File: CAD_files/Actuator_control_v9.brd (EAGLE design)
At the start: 33.5 x 16 mm, 35 parts, among them Y1 16MHz

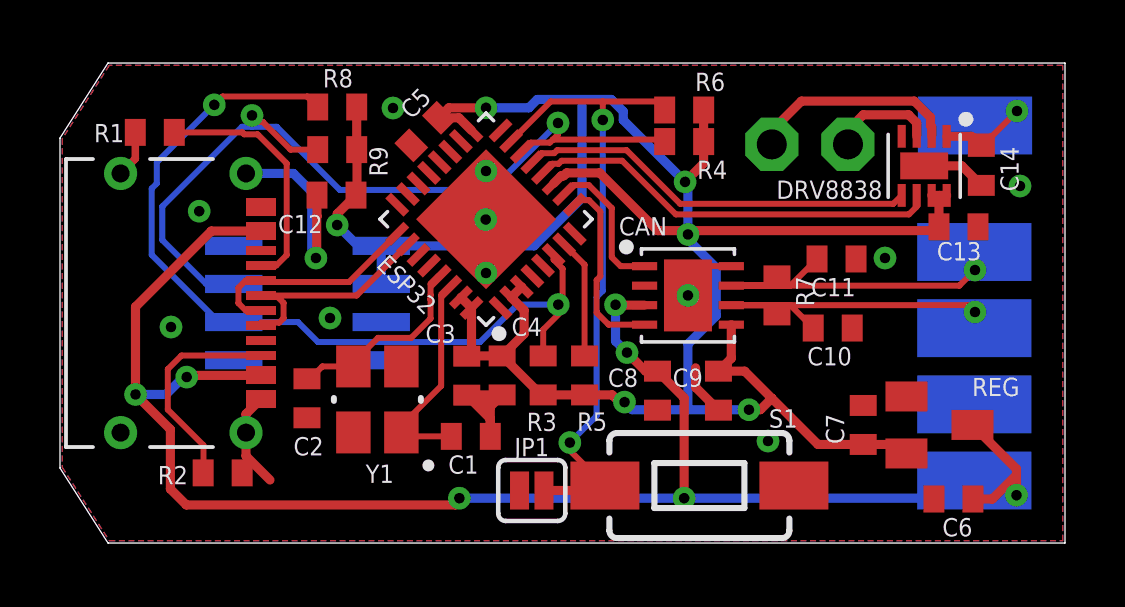
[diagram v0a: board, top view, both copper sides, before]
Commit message: Resolved issue #9
Removed CAN lines capacitors and added info regarding terminating resistors
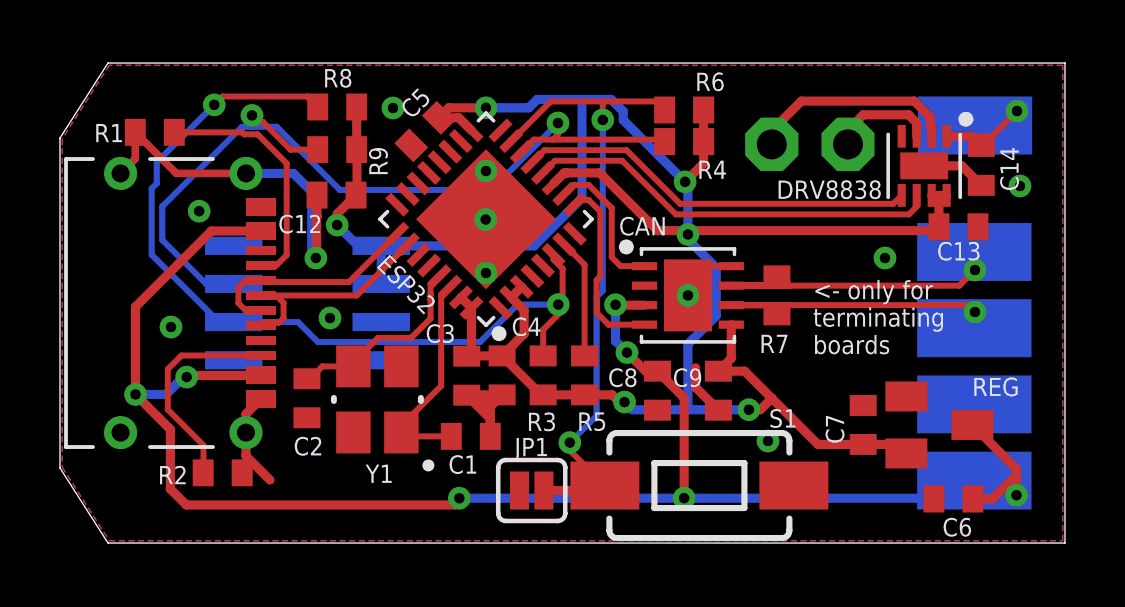
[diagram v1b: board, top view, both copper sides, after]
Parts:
- removed C10, C11: 47nF, resistor:C0402
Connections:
- net CANH: no longer C11.2
- net CANL: no longer C10.2
- net GND: no longer C10.1, C11.1
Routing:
- net GND: track 23.0 -> 27.2 mm
- net CANH: track 13.8 -> 12.6 mm
- net CANL: track 13.5 -> 12.4 mm
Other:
- board text added: "<- only for terminating boards"
